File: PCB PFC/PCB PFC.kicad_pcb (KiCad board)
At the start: 2 copper layers, 43 parts, among them J1 INA_1, J2 INA_2, J3 NMJ6HHD2, J4 External_Power, J5 BAT54S_1, J6 BAT54S_2, SW2 SW_Push, U2 L7805, U3 TL082, U4 TL084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

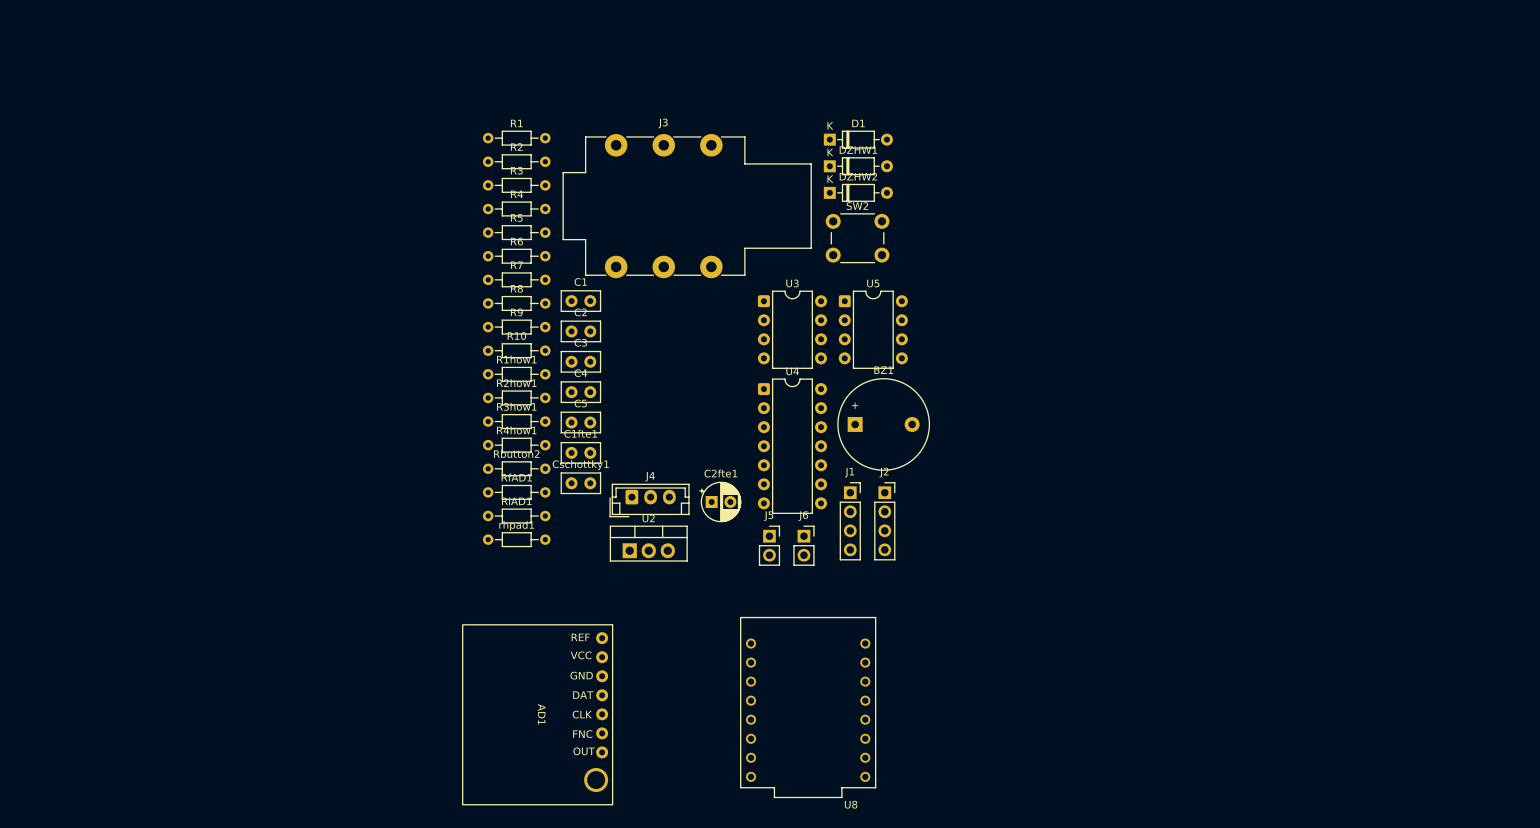
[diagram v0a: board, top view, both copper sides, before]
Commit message: Agrego jacks de ECG y librerias
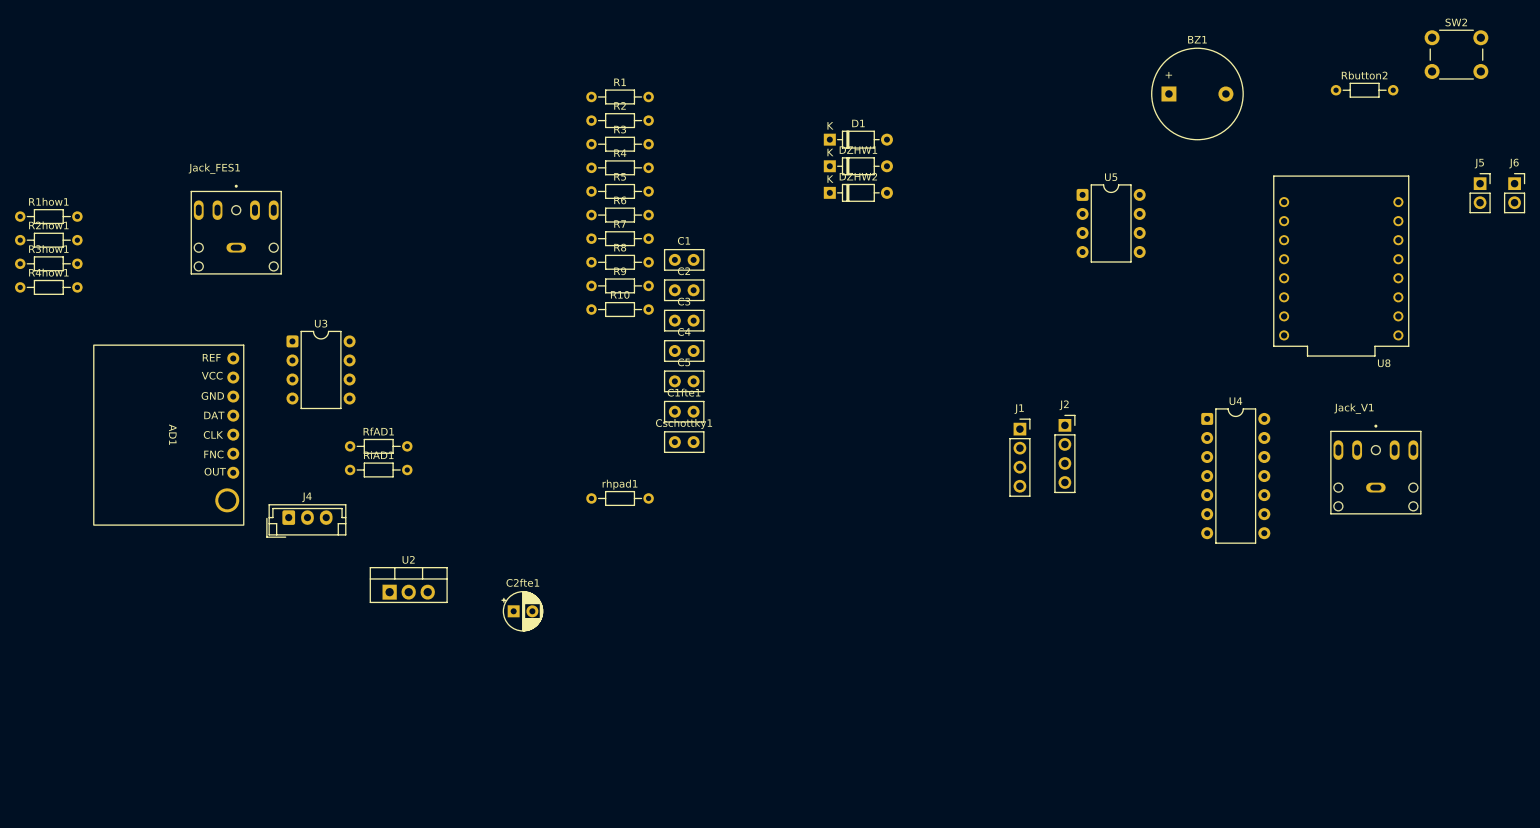
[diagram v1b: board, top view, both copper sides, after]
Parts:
- removed J3: NMJ6HHD2, Connector_Audio:Jack_6.35mm_Neutrik_NMJ6HHD2_Horizontal
- added Jack_FES1: SJ1-3525N, SJ1-3525N:CUI_SJ1-3525N, F.Cu at (73.0, 81.0)
- added Jack_V1: SJ1-3525N, SJ1-3525N:CUI_SJ1-3525N, F.Cu at (225.0, 113.0)
- moved Rbutton2 123.8 mm to (219.7, 60.0)
- moved J5 105.8 mm to (238.9, 72.5)
- moved J6 105.8 mm to (243.5, 72.5)
- moved U8 92.3 mm to (220.4, 82.8)
- moved SW2 83.5 mm to (232.5, 53.0)
- moved R1how1 65.9 mm to (44.2, 76.8)
- moved R2how1 65.9 mm to (44.2, 80.0)
- moved R3how1 65.9 mm to (44.2, 83.2)
- moved R4how1 65.9 mm to (44.2, 86.3)
- moved U3 63.1 mm to (80.5, 93.5)
- moved AD1 61.7 mm to (64.0, 106.0)
- moved BZ1 60.8 mm to (197.4, 60.5)
- moved U4 59.3 mm to (202.5, 103.8)
- moved J4 45.9 mm to (80.0, 117.0)
- moved U5 34.7 mm to (185.9, 74.0)
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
